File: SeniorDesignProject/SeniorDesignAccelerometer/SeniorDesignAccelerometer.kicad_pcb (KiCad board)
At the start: 2 copper layers, 6 parts, among them J1 EV3635A, J2 RJ45

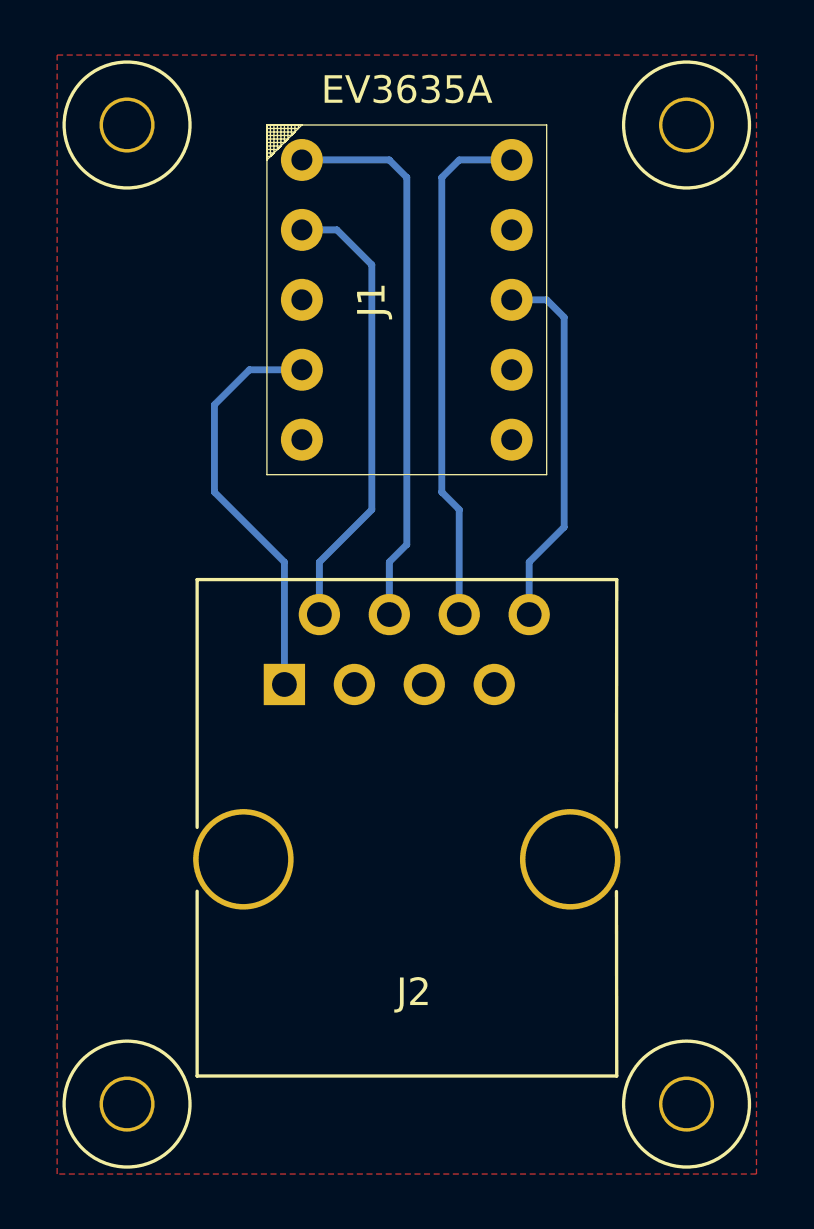
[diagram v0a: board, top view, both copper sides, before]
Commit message: Updates to accelerometer board and main board
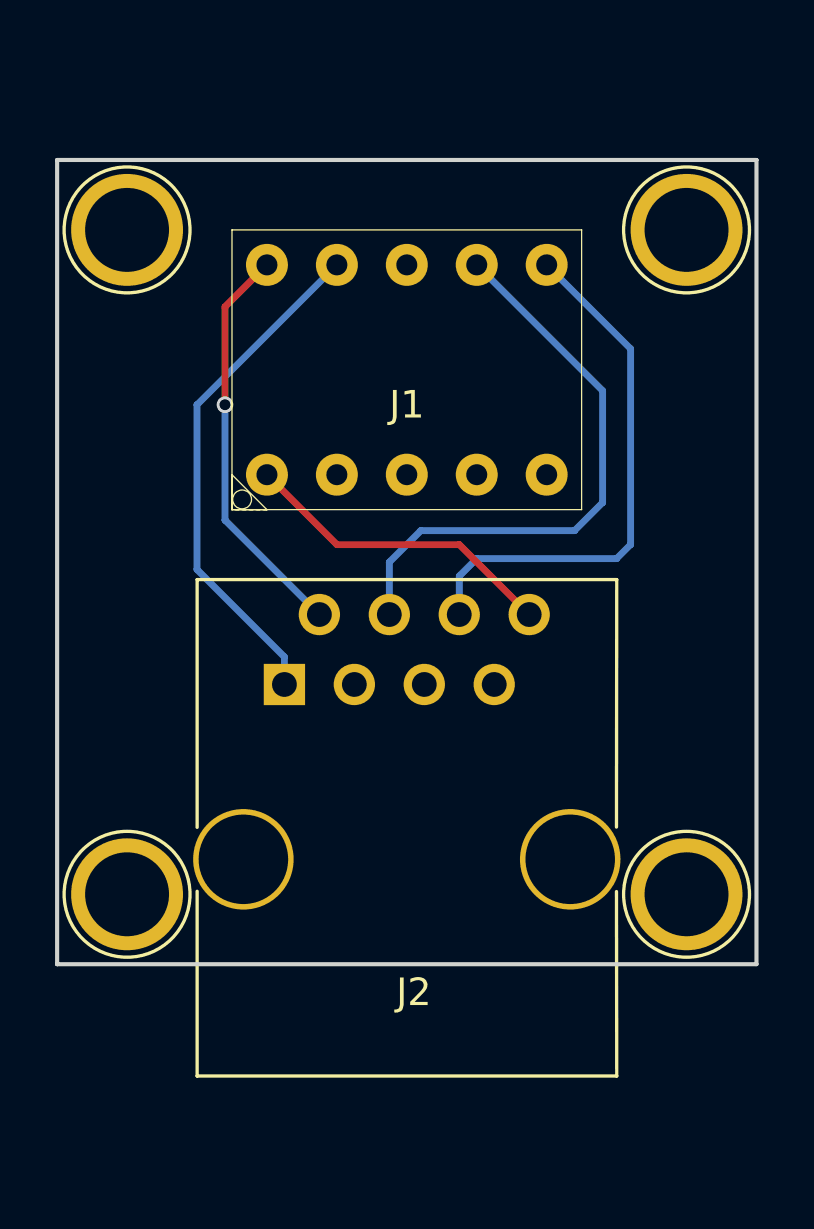
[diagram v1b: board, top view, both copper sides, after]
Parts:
- moved REF** 7.62 mm to (162.6, 111.8)
- moved REF** 7.62 mm to (142.2, 111.8)
- moved REF** 3.81 mm to (162.6, 87.6)
- moved REF** 3.81 mm to (142.2, 87.6)
- moved J1 1.80 mm to (152.4, 91.4), turned to 90 degrees
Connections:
- J1 pad 1: SDO(MISO) -> MISO
- J1 pad 10: SCL(SCK) -> SS
- J1 pad 2: SCS(CSN)(SS) -> TEST
- J1 pad 3: TEST -> AVDD
- J1 pad 4: DVDD -> VPP
- J1 pad 5: AVDD -> INT
- J1 pad 6: GND -> SCK
- J1 pad 7: VPP -> MOSI
- J1 pad 8: SDA(MOSI) -> GND
- J1 pad 9: INT -> +3.3V
- J2 pad 1: DVDD -> +3.3V
- J2 pad 2: SCS(CSN)(SS) -> SS
- J2 pad 4: SDO(MISO) -> MOSI
- J2 pad 6: SCL(SCK) -> SCK
- J2 pad 8: SDA(MOSI) -> MISO
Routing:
- net MOSI: track 0.00 -> 21.1 mm
- net SDO(MISO): track 20.2 -> 0.00 mm
- net SCK: track 0.00 -> 19.5 mm
- net SCL(SCK): track 18.9 -> 0.00 mm
- net +3.3V: track 0.00 -> 18.7 mm
- net SCS(CSN)(SS): track 16.6 -> 0.00 mm
- net DVDD: track 14.9 -> 0.00 mm
- net SS: track 0.00 -> 14.8 mm, vias 0 -> 1
- net SDA(MOSI): track 13.5 -> 0.00 mm
- net MISO: track 0.00 -> 11.6 mm
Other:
- board outline added: 25.4 x 29.2 mm
